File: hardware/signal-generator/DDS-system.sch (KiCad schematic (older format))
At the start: 19 parts, among them U1 74HC04, U10 MCP23017-E/SO, U11 AD9764AR, U12 TS4061AICT-1.25, U8 DS1085Z-10+, U9 CY7C1021D-10ZSXI

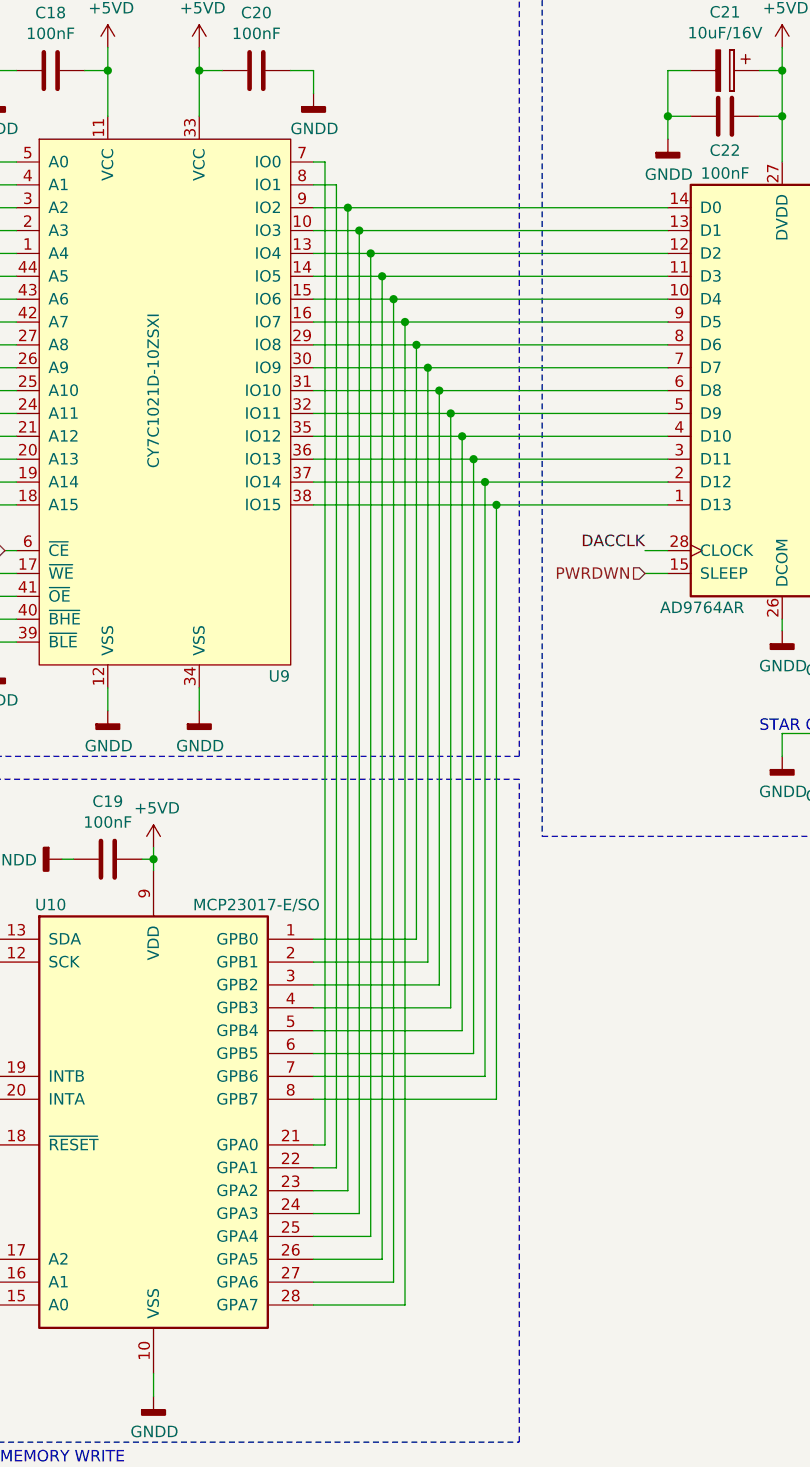
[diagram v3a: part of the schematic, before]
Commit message: [Signal Generator] Complete DDS system layout
The I/O expander (MCP23017) has been added and routed.
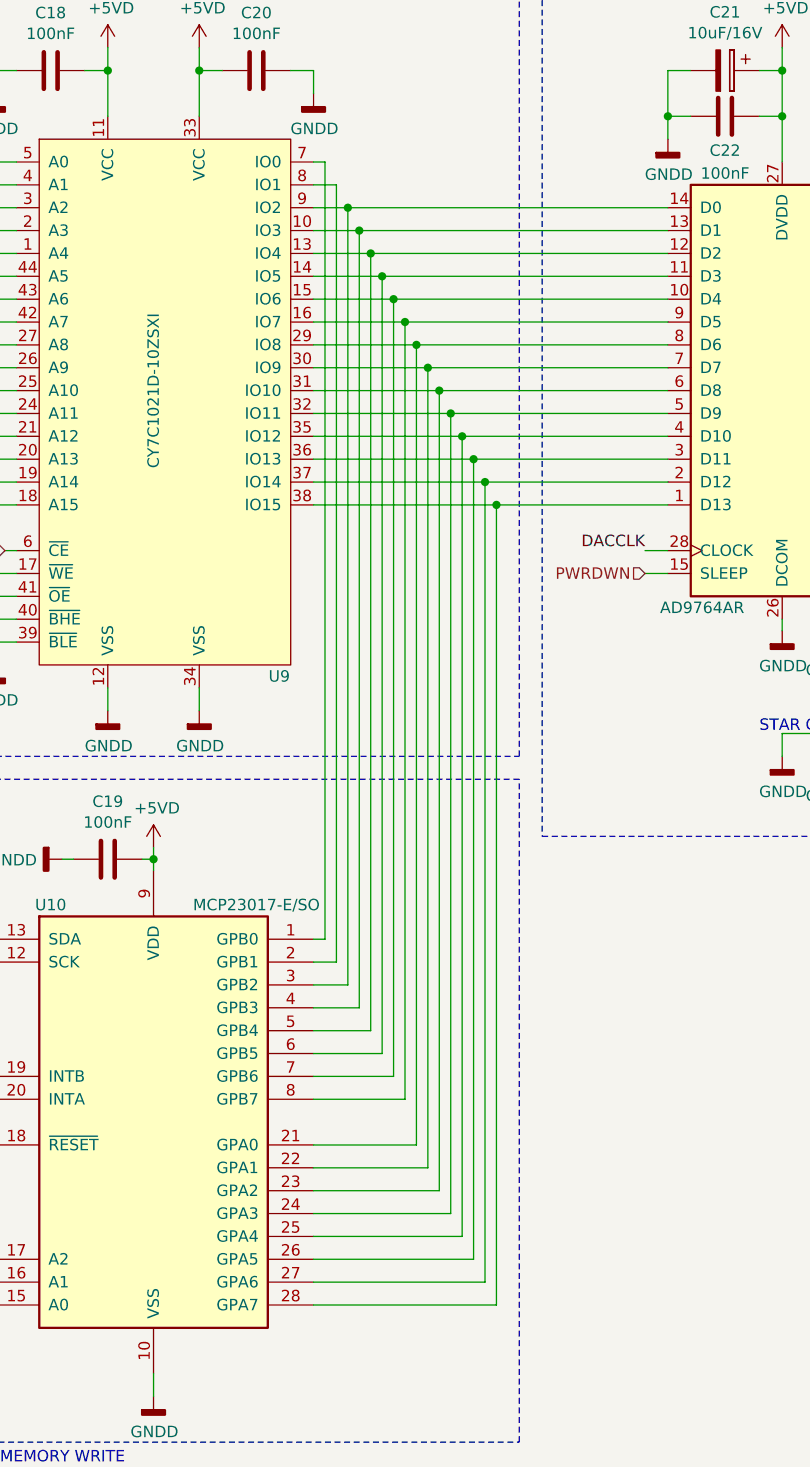
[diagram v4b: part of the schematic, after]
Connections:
- net at U11.8 (D6), U9.29 (IO8): now also U10.21 (GPA0); no longer U10.1 (GPB0)
- net at U11.7 (D7), U9.30 (IO9): now also U10.22 (GPA1); no longer U10.2 (GPB1)
- net at U9.7 (IO0): now also U10.1 (GPB0); no longer U10.21 (GPA0)
- net at U9.8 (IO1): now also U10.2 (GPB1); no longer U10.22 (GPA1)
- net at U11.14 (D0), U9.9 (IO2): now also U10.3 (GPB2); no longer U10.23 (GPA2)
- net at U11.13 (D1), U9.10 (IO3): now also U10.4 (GPB3); no longer U10.24 (GPA3)
- net at U11.12 (D2), U9.13 (IO4): now also U10.5 (GPB4); no longer U10.25 (GPA4)
- net at U11.11 (D3), U9.14 (IO5): now also U10.6 (GPB5); no longer U10.26 (GPA5)
- net at U11.10 (D4), U9.15 (IO6): now also U10.7 (GPB6); no longer U10.27 (GPA6)
- net at U11.9 (D5), U9.16 (IO7): now also U10.8 (GPB7); no longer U10.28 (GPA7)
- net at U11.6 (D8), U9.31 (IO10): now also U10.23 (GPA2); no longer U10.3 (GPB2)
- net at U11.5 (D9), U9.32 (IO11): now also U10.24 (GPA3); no longer U10.4 (GPB3)
- net at U11.4 (D10), U9.35 (IO12): now also U10.25 (GPA4); no longer U10.5 (GPB4)
- net at U11.3 (D11), U9.36 (IO13): now also U10.26 (GPA5); no longer U10.6 (GPB5)
- net at U11.2 (D12), U9.37 (IO14): now also U10.27 (GPA6); no longer U10.7 (GPB6)
- net at U11.1 (D13), U9.38 (IO15): now also U10.28 (GPA7); no longer U10.8 (GPB7)
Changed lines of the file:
@@
 Sheet 2 5
 Title "Digital Function Generator v2 - DDS System"
-Date "2019-12-20"
+Date "2019-12-28"
 Rev "1"
 Comp "Petar Nikolov"
@@
 	4550 1100 4650 1100
 Wire Wire Line
-	5950 1700 6100 1700
-Wire Wire Line
-	5950 1800 6150 1800
-Wire Wire Line
-	5950 1900 6200 1900
-Wire Wire Line
-	5950 2000 6250 2000
-Wire Wire Line
-	5950 2100 6300 2100
-Wire Wire Line
-	5950 2200 6350 2200
-Wire Wire Line
-	5950 2300 6400 2300
-Wire Wire Line
-	5950 2400 6450 2400
-Wire Wire Line
-	5950 2500 6500 2500
-Wire Wire Line
-	5950 2600 6550 2600
-Wire Wire Line
-	5950 2700 6600 2700
-Wire Wire Line
-	5950 2800 6650 2800
-Wire Wire Line
-	5950 2900 6700 2900
-Wire Wire Line
-	5950 3000 6750 3000
-Wire Wire Line
 	5950 1500 6000 1500
 Wire Wire Line
@@
 Wire Wire Line
 	4550 5000 4450 5000
-Wire Wire Line
-	6000 5800 5950 5800
-Wire Wire Line
-	6000 1500 6000 5800
-Wire Wire Line
-	5950 5900 6050 5900
-Wire Wire Line
-	6050 1600 6050 5900
-Wire Wire Line
-	6100 6000 5950 6000
-Wire Wire Line
-	6100 1700 6100 6000
-Wire Wire Line
-	5950 6100 6150 6100
-Wire Wire Line
-	6150 1800 6150 6100
-Wire Wire Line
-	6200 6200 5950 6200
-Wire Wire Line
-	6200 1900 6200 6200
-Wire Wire Line
-	5950 6300 6250 6300
-Wire Wire Line
-	6250 2000 6250 6300
-Wire Wire Line
-	6300 6400 5950 6400
-Wire Wire Line
-	6300 2100 6300 6400
-Wire Wire Line
-	5950 6500 6350 6500
-Wire Wire Line
-	6350 2200 6350 6500
-Wire Wire Line
-	6400 4900 5950 4900
-Wire Wire Line
-	6400 2300 6400 4900
-Wire Wire Line
-	5950 5000 6450 5000
-Wire Wire Line
-	6450 2400 6450 5000
-Wire Wire Line
-	6500 5100 5950 5100
-Wire Wire Line
-	6500 2500 6500 5100
-Wire Wire Line
-	5950 5200 6550 5200
-Wire Wire Line
-	6550 2600 6550 5200
-Wire Wire Line
-	6600 5300 5950 5300
-Wire Wire Line
-	6600 2700 6600 5300
-Wire Wire Line
-	5950 5400 6650 5400
-Wire Wire Line
-	6650 2800 6650 5400
-Wire Wire Line
-	6700 5500 5950 5500
-Wire Wire Line
-	6700 2900 6700 5500
-Wire Wire Line
-	5950 5600 6750 5600
-Wire Wire Line
-	6750 3000 6750 5600
 $Comp
 L power:GNDD #PWR056
@@
 Text Label 2150 3100 1    50   ~ 0
 DACCLK
-Wire Wire Line
-	6100 1700 7500 1700
-Connection ~ 6100 1700
-Wire Wire Line
-	6150 1800 7500 1800
-Connection ~ 6150 1800
-Wire Wire Line
-	6200 1900 7500 1900
-Connection ~ 6200 1900
-Wire Wire Line
-	6250 2000 7500 2000
-Connection ~ 6250 2000
-Wire Wire Line
-	6300 2100 7500 2100
-Connection ~ 6300 2100
-Wire Wire Line
-	6350 2200 7500 2200
-Connection ~ 6350 2200
-Wire Wire Line
-	6400 2300 7500 2300
-Connection ~ 6400 2300
-Wire Wire Line
-	6700 2900 7500 2900
-Connection ~ 6700 2900
-Wire Wire Line
-	6650 2800 7500 2800
-Connection ~ 6650 2800
-Wire Wire Line
-	6600 2700 7500 2700
-Connection ~ 6600 2700
-Wire Wire Line
-	6550 2600 7500 2600
-Connection ~ 6550 2600
-Wire Wire Line
-	6500 2500 7500 2500
-Connection ~ 6500 2500
-Wire Wire Line
-	6450 2400 7500 2400
-Connection ~ 6450 2400
-Wire Wire Line
-	6750 3000 7500 3000
-Connection ~ 6750 3000
 $Comp
 L power:+5VA #PWR071
@@
 Wire Notes Line
 	6950 750  10050 750
+Wire Wire Line
+	5950 1700 6100 1700
+Wire Wire Line
+	5950 1800 6150 1800
+Wire Wire Line
+	5950 1900 6200 1900
+Wire Wire Line
+	5950 2000 6250 2000
+Wire Wire Line
+	5950 2100 6300 2100
+Wire Wire Line
+	5950 2200 6350 2200
+Wire Wire Line
+	5950 2300 6400 2300
+Wire Wire Line
+	5950 2400 6450 2400
+Wire Wire Line
+	5950 2500 6500 2500
+Wire Wire Line
+	5950 2600 6550 2600
+Wire Wire Line
+	5950 2700 6600 2700
+Wire Wire Line
+	5950 2800 6650 2800
+Wire Wire Line
+	5950 2900 6700 2900
+Wire Wire Line
+	5950 3000 6750 3000
+Wire Wire Line
+	5950 5800 6400 5800
+Wire Wire Line
+	5950 5900 6450 5900
+Wire Wire Line
+	5950 6000 6500 6000
+Wire Wire Line
+	5950 6100 6550 6100
+Wire Wire Line
+	5950 6200 6600 6200
+Wire Wire Line
+	5950 6300 6650 6300
+Wire Wire Line
+	5950 6400 6700 6400
+Wire Wire Line
+	5950 6500 6750 6500
+Wire Wire Line
+	5950 4900 6000 4900
+Wire Wire Line
+	5950 5000 6050 5000
+Wire Wire Line
+	5950 5100 6100 5100
+Wire Wire Line
+	5950 5200 6150 5200
+Wire Wire Line
+	5950 5300 6200 5300
+Wire Wire Line
+	5950 5400 6250 5400
+Wire Wire Line
+	5950 5500 6300 5500
+Wire Wire Line
+	5950 5600 6350 5600
+Wire Wire Line
+	6000 4900 6000 1500
+Wire Wire Line
+	6050 1600 6050 5000
+Wire Wire Line
+	6100 5100 6100 1700
+Connection ~ 6100 1700
+Wire Wire Line
+	6100 1700 7500 1700
+Wire Wire Line
+	6150 1800 6150 5200
+Connection ~ 6150 1800
+Wire Wire Line
+	6150 1800 7500 1800
+Wire Wire Line
+	6200 5300 6200 1900
+Connection ~ 6200 1900
+Wire Wire Line
+	6200 1900 7500 1900
+Wire Wire Line
+	6250 2000 6250 5400
+Connection ~ 6250 2000
+Wire Wire Line
+	6250 2000 7500 2000
+Wire Wire Line
+	6300 5500 6300 2100
+Connection ~ 6300 2100
+Wire Wire Line
+	6300 2100 7500 2100
+Wire Wire Line
+	6350 2200 6350 5600
+Connection ~ 6350 2200
+Wire Wire Line
+	6350 2200 7500 2200
+Wire Wire Line
+	6400 5800 6400 2300
+Connection ~ 6400 2300
+Wire Wire Line
+	6400 2300 7500 2300
+Wire Wire Line
+	6450 2400 6450 5900
+Connection ~ 6450 2400
+Wire Wire Line
+	6450 2400 7500 2400
+Wire Wire Line
+	6500 6000 6500 2500
+Connection ~ 6500 2500
+Wire Wire Line
+	6500 2500 7500 2500
+Wire Wire Line
+	6550 2600 6550 6100
+Connection ~ 6550 2600
+Wire Wire Line
+	6550 2600 7500 2600
+Wire Wire Line
+	6600 6200 6600 2700
+Connection ~ 6600 2700
+Wire Wire Line
+	6600 2700 7500 2700
+Wire Wire Line
+	6650 2800 6650 6300
+Connection ~ 6650 2800
+Wire Wire Line
+	6650 2800 7500 2800
+Wire Wire Line
+	6700 6400 6700 2900
+Connection ~ 6700 2900
+Wire Wire Line
+	6700 2900 7500 2900
+Wire Wire Line
+	6750 3000 6750 6500
+Connection ~ 6750 3000
+Wire Wire Line
+	6750 3000 7500 3000
 $EndSCHEMATC

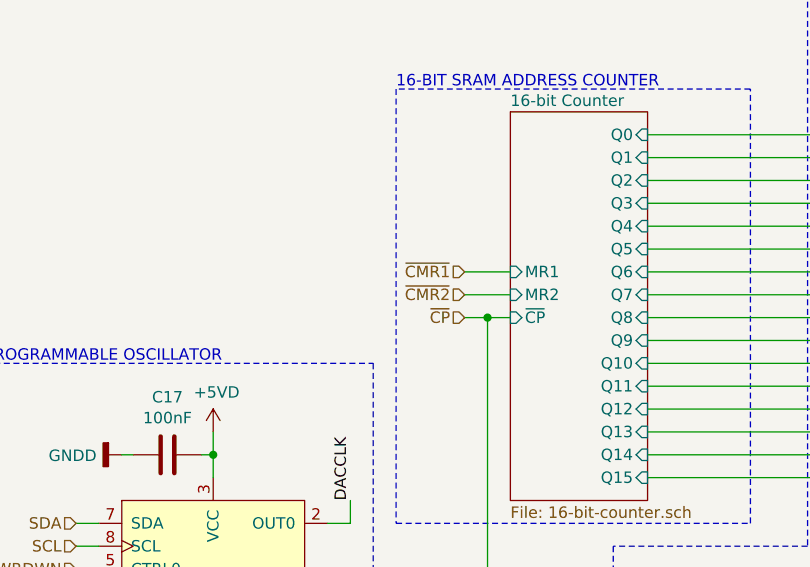
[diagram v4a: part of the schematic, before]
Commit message: [Signal Generator] Change notation of counter reset signals
~CMR1 -> CMR1
~CMR2 -> CMR2
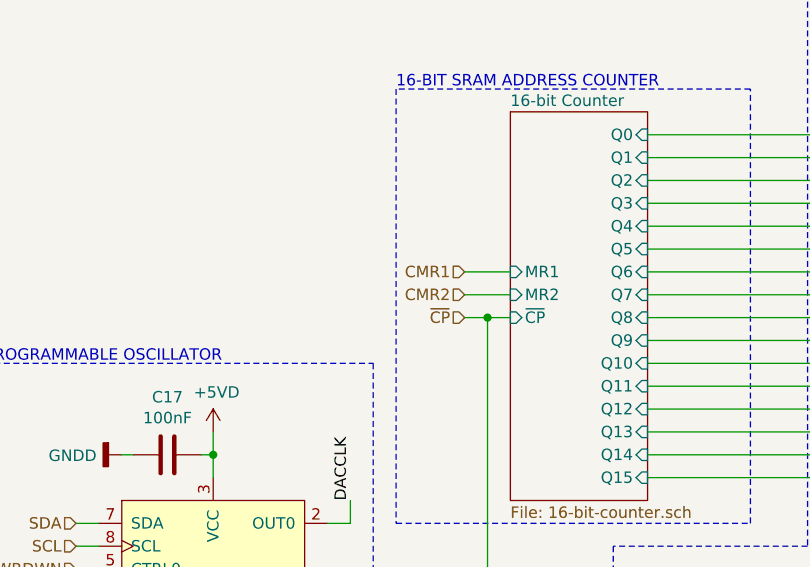
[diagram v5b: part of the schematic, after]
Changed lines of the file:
@@
 Sheet 2 5
 Title "Digital Function Generator v2 - DDS System"
-Date "2019-12-28"
+Date "2020-01-19"
 Rev "1"
 Comp "Petar Nikolov"
@@
 	2850 2200 2650 2200
 Text HLabel 2650 2100 0    50   Input ~ 0
-~CMR1
+CMR1
 Text HLabel 2650 2200 0    50   Input ~ 0
-~CMR2
+CMR2
 Wire Wire Line
 	4650 3200 4600 3200
